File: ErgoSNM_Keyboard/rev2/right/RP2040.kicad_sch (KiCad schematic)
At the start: 28 parts, among them SW1 BOOT, SW2 RESET, U3 W25Q128JVS, U4 RP2040, Y1 12MHz

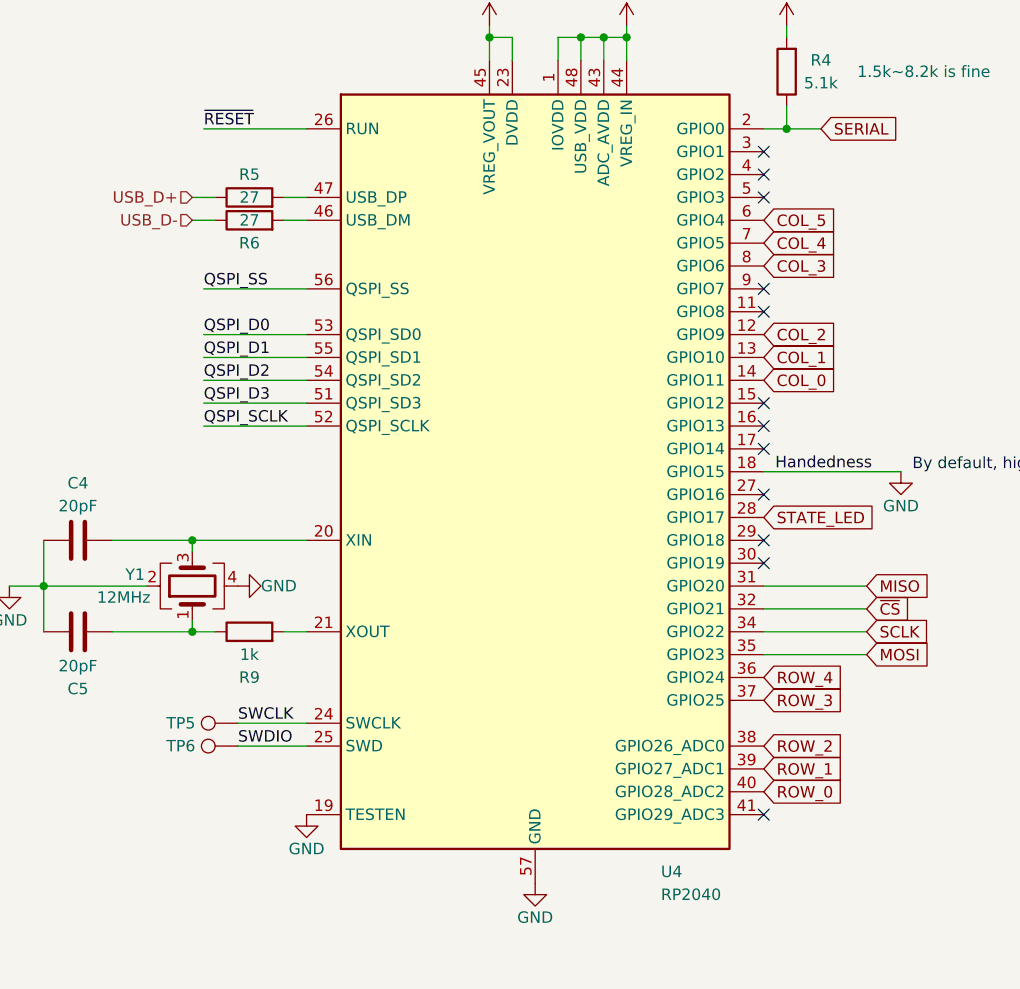
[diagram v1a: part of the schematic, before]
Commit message: Update right PCB
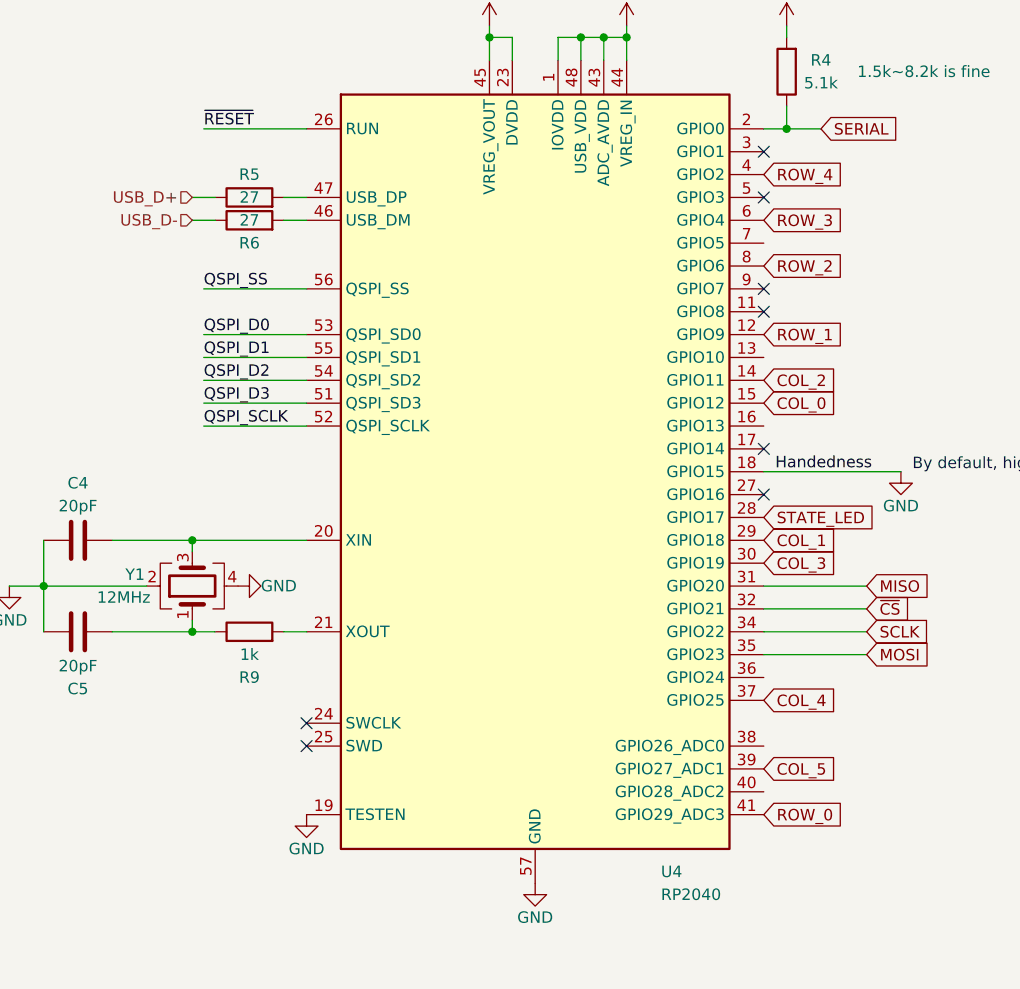
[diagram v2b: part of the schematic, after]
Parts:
- removed TP5, TP6: TestPoint, TestPoint:TestPoint_Pad_D2.5mm, symbol Connector:TestPoint
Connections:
- net COL_0: now also U4.15 (GPIO12); no longer U4.14 (GPIO11)
- net COL_1: now also U4.29 (GPIO18); no longer U4.13 (GPIO10)
- net COL_2: now also U4.14 (GPIO11); no longer U4.12 (GPIO9)
- net COL_3: now also U4.30 (GPIO19); no longer U4.8 (GPIO6)
- net COL_4: now also U4.37 (GPIO25); no longer U4.7 (GPIO5)
- net COL_5: now also U4.39 (GPIO27_ADC1); no longer U4.6 (GPIO4)
- net ROW_0: now also U4.41 (GPIO29_ADC3); no longer U4.40 (GPIO28_ADC2)
- net ROW_1: now also U4.12 (GPIO9); no longer U4.39 (GPIO27_ADC1)
- net ROW_2: now also U4.8 (GPIO6); no longer U4.38 (GPIO26_ADC0)
- net ROW_3: now also U4.6 (GPIO4); no longer U4.37 (GPIO25)
- net ROW_4: now also U4.4 (GPIO2); no longer U4.36 (GPIO24)
- net SWCLK: no longer names the net of U4.24 (SWCLK)
- net SWDIO: no longer names the net of U4.25 (SWD)
- no-connect marks 12 -> 8
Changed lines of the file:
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@@
   )
   (no_connect (at 114.3 77.47))
-  (no_connect (at 114.3 67.31))
-  (no_connect (at 114.3 69.85))
   (no_connect (at 114.3 72.39))
-  (no_connect (at 114.3 85.09))
-  (no_connect (at 114.3 113.03))
   (no_connect (at 114.3 57.15))
   (no_connect (at 114.3 54.61))
   (no_connect (at 114.3 44.45))
-  (no_connect (at 114.3 41.91))
   (no_connect (at 114.3 39.37))
-  (no_connect (at 114.3 82.55))
+  (no_connect (at 63.5 102.87))
+  (no_connect (at 63.5 105.41))
   (wire (pts (xy 242.57 120.65) (xy 242.57 119.38))
     (stroke (width 0) (type default) (color 0 0 0 0))
@@
     (stroke (width 0) (type default) (color 0 0 0 0))
   )
-  (wire (pts (xy 55.88 102.87) (xy 63.5 102.87))
-    (stroke (width 0) (type default) (color 0 0 0 0))
-  )
   (wire (pts (xy 189.23 59.69) (xy 213.36 59.69))
     (stroke (width 0) (type default) (color 0 0 0 0))
@@
   )
   (wire (pts (xy 116.84 25.4) (xy 116.84 26.67))
-    (stroke (width 0) (type default) (color 0 0 0 0))
-  )
-  (wire (pts (xy 55.88 105.41) (xy 63.5 105.41))
     (stroke (width 0) (type default) (color 0 0 0 0))
   )
@@
     (effects (font (size 1.27 1.27)) (justify left bottom))
   )
-  (label "SWCLK" (at 55.88 102.87 0)
-    (effects (font (size 1.27 1.27)) (justify left bottom))
-  )
-  (label "SWDIO" (at 55.88 105.41 0)
-    (effects (font (size 1.27 1.27)) (justify left bottom))
-  )
   (label "~{RESET}" (at 52.07 36.83 0)
     (effects (font (size 1.27 1.27)) (justify left bottom))
@@
     (effects (font (size 1.27 1.27)) (justify left bottom))
   )
-  (global_label "COL_5" (shape input) (at 114.3 46.99 0) (fields_autoplaced)
-    (effects (font (size 1.27 1.27)) (justify left))
-    (property "Intersheet References" "${INTERSHEET_REFS}" (id 0) (at 122.5188 47.0694 0)
-      (effects (font (size 1.27 1.27)) (justify left) hide)
-    )
-  )
-  (global_label "ROW_2" (shape input) (at 114.3 105.41 0) (fields_autoplaced)
-    (effects (font (size 1.27 1.27)) (justify left))
-    (property "Intersheet References" "${INTERSHEET_REFS}" (id 0) (at 122.9421 105.4894 0)
-      (effects (font (size 1.27 1.27)) (justify left) hide)
-    )
-  )
-  (global_label "COL_2" (shape input) (at 114.3 59.69 0) (fields_autoplaced)
-    (effects (font (size 1.27 1.27)) (justify left))
-    (property "Intersheet References" "${INTERSHEET_REFS}" (id 0) (at 122.5188 59.7694 0)
-      (effects (font (size 1.27 1.27)) (justify left) hide)
-    )
-  )
-  (global_label "COL_4" (shape input) (at 114.3 49.53 0) (fields_autoplaced)
-    (effects (font (size 1.27 1.27)) (justify left))
-    (property "Intersheet References" "${INTERSHEET_REFS}" (id 0) (at 122.5188 49.6094 0)
-      (effects (font (size 1.27 1.27)) (justify left) hide)
-    )
-  )
-  (global_label "ROW_3" (shape input) (at 114.3 100.33 0) (fields_autoplaced)
-    (effects (font (size 1.27 1.27)) (justify left))
-    (property "Intersheet References" "${INTERSHEET_REFS}" (id 0) (at 122.9421 100.4094 0)
+  (global_label "COL_5" (shape input) (at 114.3 107.95 0) (fields_autoplaced)
+    (effects (font (size 1.27 1.27)) (justify left))
+    (property "Intersheet References" "${INTERSHEET_REFS}" (id 0) (at 122.5188 108.0294 0)
+      (effects (font (size 1.27 1.27)) (justify left) hide)
+    )
+  )
+  (global_label "ROW_2" (shape input) (at 114.3 52.07 0) (fields_autoplaced)
+    (effects (font (size 1.27 1.27)) (justify left))
+    (property "Intersheet References" "${INTERSHEET_REFS}" (id 0) (at 122.9421 52.1494 0)
+      (effects (font (size 1.27 1.27)) (justify left) hide)
+    )
+  )
+  (global_label "COL_2" (shape input) (at 114.3 64.77 0) (fields_autoplaced)
+    (effects (font (size 1.27 1.27)) (justify left))
+    (property "Intersheet References" "${INTERSHEET_REFS}" (id 0) (at 122.5188 64.8494 0)
+      (effects (font (size 1.27 1.27)) (justify left) hide)
+    )
+  )
+  (global_label "COL_4" (shape input) (at 114.3 100.33 0) (fields_autoplaced)
+    (effects (font (size 1.27 1.27)) (justify left))
+    (property "Intersheet References" "${INTERSHEET_REFS}" (id 0) (at 122.5188 100.4094 0)
+      (effects (font (size 1.27 1.27)) (justify left) hide)
+    )
+  )
+  (global_label "ROW_3" (shape input) (at 114.3 46.99 0) (fields_autoplaced)
+    (effects (font (size 1.27 1.27)) (justify left))
+    (property "Intersheet References" "${INTERSHEET_REFS}" (id 0) (at 122.9421 47.0694 0)
       (effects (font (size 1.27 1.27)) (justify left) hide)
     )
@@
     )
   )
-  (global_label "ROW_0" (shape input) (at 114.3 110.49 0) (fields_autoplaced)
-    (effects (font (size 1.27 1.27)) (justify left))
-    (property "Intersheet References" "${INTERSHEET_REFS}" (id 0) (at 122.9421 110.5694 0)
+  (global_label "ROW_0" (shape input) (at 114.3 113.03 0) (fields_autoplaced)
+    (effects (font (size 1.27 1.27)) (justify left))
+    (property "Intersheet References" "${INTERSHEET_REFS}" (id 0) (at 122.9421 113.1094 0)
       (effects (font (size 1.27 1.27)) (justify left) hide)
     )
@@
     )
   )
-  (global_label "COL_0" (shape input) (at 114.3 64.77 0) (fields_autoplaced)
-    (effects (font (size 1.27 1.27)) (justify left))
-    (property "Intersheet References" "${INTERSHEET_REFS}" (id 0) (at 122.5188 64.8494 0)
+  (global_label "COL_0" (shape input) (at 114.3 67.31 0) (fields_autoplaced)
+    (effects (font (size 1.27 1.27)) (justify left))
+    (property "Intersheet References" "${INTERSHEET_REFS}" (id 0) (at 122.5188 67.3894 0)
       (effects (font (size 1.27 1.27)) (justify left) hide)
     )
@@
     )
   )
-  (global_label "ROW_4" (shape input) (at 114.3 97.79 0) (fields_autoplaced)
-    (effects (font (size 1.27 1.27)) (justify left))
-    (property "Intersheet References" "${INTERSHEET_REFS}" (id 0) (at 122.9421 97.8694 0)
-      (effects (font (size 1.27 1.27)) (justify left) hide)
-    )
-  )
-  (global_label "COL_3" (shape input) (at 114.3 52.07 0) (fields_autoplaced)
-    (effects (font (size 1.27 1.27)) (justify left))
-    (property "Intersheet References" "${INTERSHEET_REFS}" (id 0) (at 122.5188 52.1494 0)
-      (effects (font (size 1.27 1.27)) (justify left) hide)
-    )
-  )
-  (global_label "COL_1" (shape input) (at 114.3 62.23 0) (fields_autoplaced)
-    (effects (font (size 1.27 1.27)) (justify left))
-    (property "Intersheet References" "${INTERSHEET_REFS}" (id 0) (at 122.5188 62.3094 0)
+  (global_label "ROW_4" (shape input) (at 114.3 41.91 0) (fields_autoplaced)
+    (effects (font (size 1.27 1.27)) (justify left))
+    (property "Intersheet References" "${INTERSHEET_REFS}" (id 0) (at 122.9421 41.9894 0)
+      (effects (font (size 1.27 1.27)) (justify left) hide)
+    )
+  )
+  (global_label "COL_3" (shape input) (at 114.3 85.09 0) (fields_autoplaced)
+    (effects (font (size 1.27 1.27)) (justify left))
+    (property "Intersheet References" "${INTERSHEET_REFS}" (id 0) (at 122.5188 85.1694 0)
+      (effects (font (size 1.27 1.27)) (justify left) hide)
+    )
+  )
+  (global_label "COL_1" (shape input) (at 114.3 82.55 0) (fields_autoplaced)
+    (effects (font (size 1.27 1.27)) (justify left))
+    (property "Intersheet References" "${INTERSHEET_REFS}" (id 0) (at 122.5188 82.6294 0)
       (effects (font (size 1.27 1.27)) (justify left) hide)
     )
@@
     )
   )
-  (global_label "ROW_1" (shape input) (at 114.3 107.95 0) (fields_autoplaced)
-    (effects (font (size 1.27 1.27)) (justify left))
-    (property "Intersheet References" "${INTERSHEET_REFS}" (id 0) (at 122.9421 108.0294 0)
+  (global_label "ROW_1" (shape input) (at 114.3 59.69 0) (fields_autoplaced)
+    (effects (font (size 1.27 1.27)) (justify left))
+    (property "Intersheet References" "${INTERSHEET_REFS}" (id 0) (at 122.9421 59.7694 0)
       (effects (font (size 1.27 1.27)) (justify left) hide)
     )
@@
     (pin "1")
     (pin "2")
-  )
-  (symbol (lib_id "Connector:TestPoint") (at 55.88 105.41 90) (unit 1)
-    (in_bom no) (on_board yes)
-    (property "Reference" "TP6" (id 0) (at 49.53 105.41 90))
-    (property "Value" "TestPoint" (id 1) (at 46.99 106.68 90)
-      (effects (font (size 1.27 1.27)) hide)
-    )
-    (property "Footprint" "TestPoint:TestPoint_Pad_D2.5mm" (id 2) (at 55.88 100.33 0)
-      (effects (font (size 1.27 1.27)) hide)
-    )
-    (property "Datasheet" "~" (id 3) (at 55.88 100.33 0)
-      (effects (font (size 1.27 1.27)) hide)
-    )
-    (pin "1")
   )
   (symbol (lib_id "power:+3V3") (at 116.84 25.4 0) (unit 1)
@@
   (symbol (lib_id "power:GND") (at 129.54 74.93 0) (unit 1)
     (in_bom yes) (on_board yes)
-    (property "Reference" "#PWR?" (id 0) (at 129.54 81.28 0)
+    (property "Reference" "#PWR0102" (id 0) (at 129.54 81.28 0)
       (effects (font (size 1.27 1.27)) hide)
     )
@@
       (effects (font (size 1.27 1.27)) hide)
     )
-    (pin "1")
-  )
-  (symbol (lib_id "Connector:TestPoint") (at 55.88 102.87 90) (unit 1)
-    (in_bom no) (on_board yes)
-    (property "Reference" "TP5" (id 0) (at 49.53 102.87 90))
-    (property "Value" "TestPoint" (id 1) (at 46.99 104.14 90)
-      (effects (font (size 1.27 1.27)) hide)
-    )
-    (property "Footprint" "TestPoint:TestPoint_Pad_D2.5mm" (id 2) (at 55.88 97.79 0)
-      (effects (font (size 1.27 1.27)) hide)
-    )
-    (property "Datasheet" "~" (id 3) (at 55.88 97.79 0)
-      (effects (font (size 1.27 1.27)) hide)
-    )
